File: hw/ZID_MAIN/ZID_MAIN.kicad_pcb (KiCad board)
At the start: 2 copper layers, 127 x 88.9 mm, 200 parts, among them J1 Conn 1x04 0.1" Socket, J10 FFC/FPC-40 Socket, J11 JST-PH-K B6B, J14 USB-C PWR ONLY, J2 JST-PH-K B6B, J3 Conn 1x02 0.1" pin, J4 Conn 1x03 0.1" pin, J5 Conn 1x08 0.1" pin, J6 Conn 1x08 0.1" pin, J7 Conn 2x04 0.1" pin, J8 Conn 2x02 0.1" pin, J9 Conn 2x04 0.1" pin, M1 WS-RP2040-Zero, SW1 SW_Push, SW2 SW_DIP_x02, U1 OSC-20MHz, U10 27WZ06, U11 74LVC125AS, U12 74LVC273, U13 74FCT2245, U14 AS7C1024B, U16 74FCT2245, U18 ATF1508AS, U2 74FCT2245, U20 74FCT2244, U22 ATF1504AS-44T, U23 74AHCT00, U24 74FCT2244, U25 ATF1504AS-44T, U26 ATF1504AS-44T, U27 ATF1504AS-44T, U28 ATF1504AS-44T, U3 24LC32, U4 MIC2775, U5 SST39SF010, U6 74LVC245, U7 74FCT2245, U8 74AHCT14, U9 Z80 C20MHz-PLCC

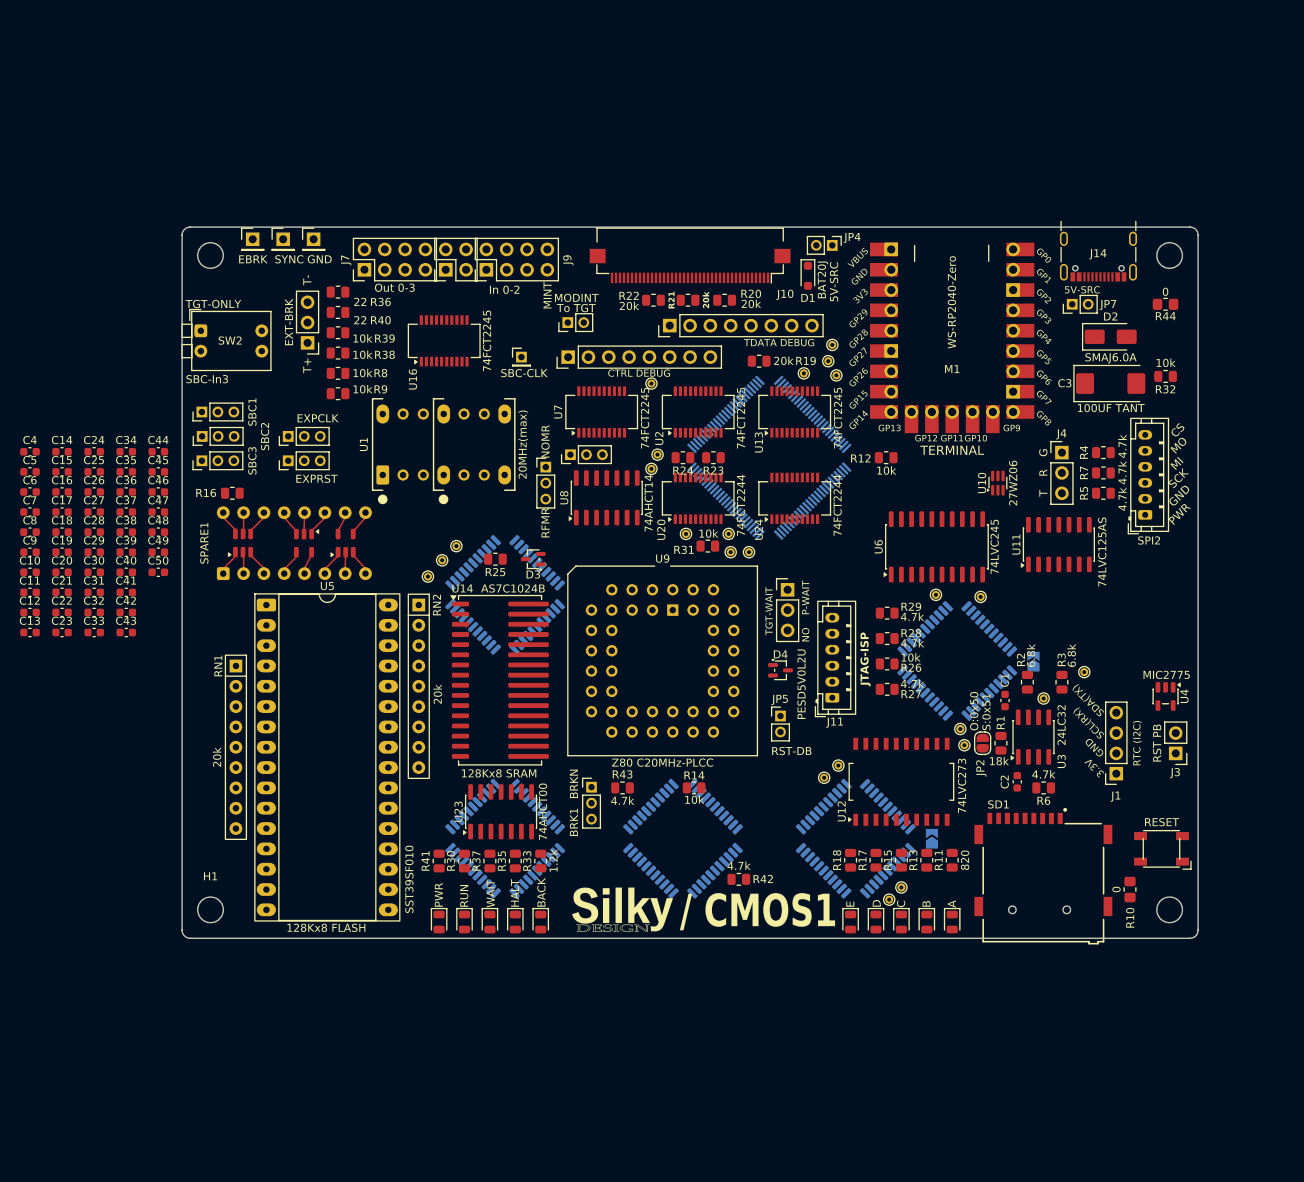
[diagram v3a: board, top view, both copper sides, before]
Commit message: SCHM: Updates per SM. PLD: comment corrections. PCB: start routing.
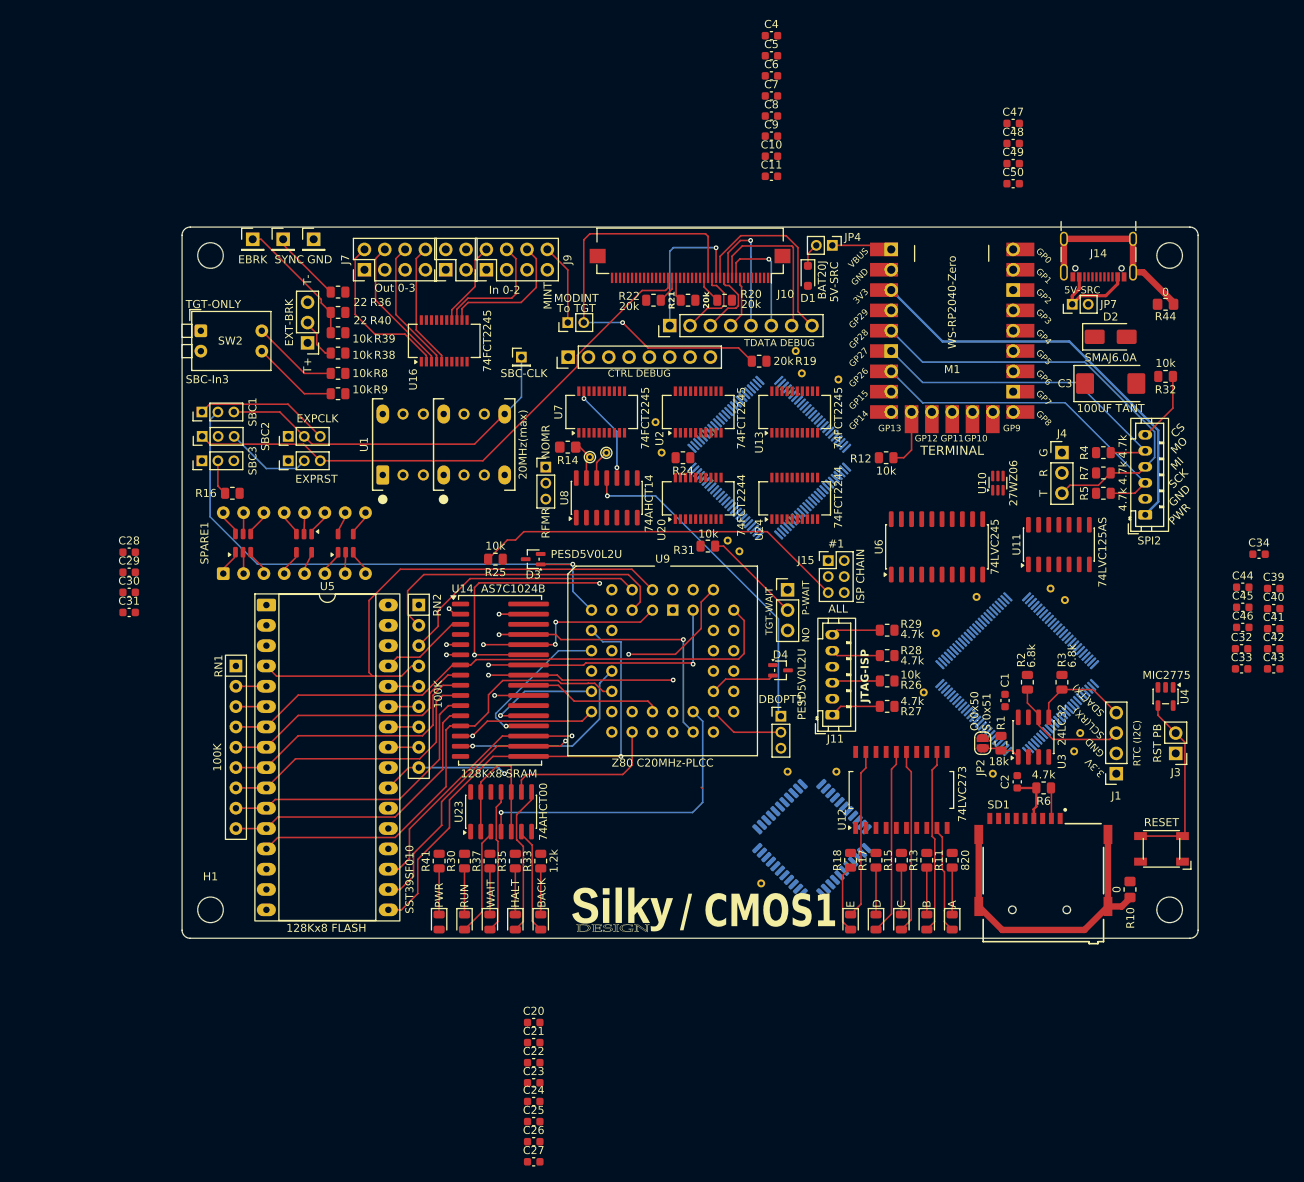
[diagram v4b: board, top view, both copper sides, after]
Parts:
- removed C12, C13, C14, C15, C16, C17, C18, C19, C35, C36, C37, C38: 0.1uF, Capacitor_SMD:C_0603_1608Metric
- removed JC1, JD1: SolderJumper_2_Open, Jumper:SolderJumper-2_P1.3mm_Open_TrianglePad1.0x1.5mm
- removed JP5: Jumper_2_Small_Bridged, Connector_PinHeader_2.00mm:PinHeader_1x02_P2.00mm_Vertical
- removed OP4: AES-Option_A-B_2mm, Connector_PinHeader_2.00mm:PinHeader_1x03_P2.00mm_Vertical
- removed R23: 10k, Resistor_SMD:R_0805_2012Metric
- removed R42, R43: 4.7k, Resistor_SMD:R_0805_2012Metric
- removed SPRU8F1: Conn_01x03_Pin, Connector_PinHeader_2.00mm:PinHeader_1x03_P2.00mm_Vertical
- removed TP12, TP26, TP28, TP29, TP31, TP32, TP33, TP34: TestPoint, TestPoint:TestPoint_THTPad_D1.0mm_Drill0.5mm
- removed U25, U26, U27, U28: ATF1504AS-44T, Package_QFP:TQFP-44_10x10mm_P0.8mm
- added DBOPT1: AES-Option_A-B_2mm, Connector_PinHeader_2.00mm:PinHeader_1x03_P2.00mm_Vertical, F.Cu at (133.6, 117.0)
- added J15: Conn 2x03 pin hdr 0.1", Connector_PinHeader_2.00mm:PinHeader_2x03_P2.00mm_Vertical, F.Cu at (139.5, 97.6)
- added TP19: TestPoint, TestPoint:TestPoint_THTPad_D1.0mm_Drill0.5mm, B.Cu at (170.2, 121.4)
- added TP20: TestPoint, TestPoint:TestPoint_THTPad_D1.0mm_Drill0.5mm, B.Cu at (134.4, 124.0)
- added TP23: TestPoint, TestPoint:TestPoint_THTPad_D1.0mm_Drill0.5mm, B.Cu at (160.1, 124.2)
- added TP24: TestPoint, TestPoint:TestPoint_THTPad_D1.0mm_Drill0.5mm, B.Cu at (153.0, 106.6)
- added U15: ATF1508AS, Package_QFP:TQFP-100_14x14mm_P0.5mm, B.Cu at (163.1, 111.8)
- R14: value 10k -> 100K; footprint Resistor_SMD:R_0805_2012Metric -> Resistor_SMD:R_0805_2012Metric_Pad1.20x1.40mm_HandSolder
- RN1, RN2: value 20k -> 100K
- TP10, TP11, TP13, TP17, TP18, TP2, TP21, TP22, TP25, TP4, TP5, TP6, TP8, TP9: moved to B.Cu
- moved C32 143.5 mm to (191.2, 108.6)
- moved C33 143.5 mm to (191.2, 111.1)
- moved C39 143.5 mm to (195.2, 101.1)
- moved C40 143.5 mm to (195.2, 103.6)
- moved C41 143.5 mm to (195.2, 106.1)
- moved C42 143.5 mm to (195.2, 108.6)
- moved C43 143.5 mm to (195.2, 111.1)
- moved C34 142.2 mm to (193.4, 96.8)
- moved C44 136.6 mm to (191.3, 100.9)
- moved C45 136.6 mm to (191.3, 103.4)
- moved C46 136.6 mm to (191.3, 105.9)
- moved C48 117.4 mm to (162.6, 45.4)
- moved C47 117.4 mm to (162.6, 42.9)
- moved C49 117.4 mm to (162.6, 47.9)
- moved C50 117.4 mm to (162.6, 50.5)
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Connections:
- net /MEM_OP- renamed /MEM_OP
- net Net-(JP7-A) renamed /VBUSP
- R14 pad 1: +5V -> Net-(R14-Pad1)
- R14 pad 2: Net-(JP5-B) -> +5V
- R25 pad 1: /PU -> +5V
- R25 pad 2: +5V -> /D2_IN
- R44 pad 1: Net-(J14-SHIELD-PadSH1) -> GND
- R44 pad 2: GND -> Net-(J14-SHIELD-PadSH1)
- TP10 pad 1: /IO85 -> Net-(U18-FMC89/IO)
- TP11 pad 1: /IO83 -> Net-(U18-FMC88/IO)
- TP13 pad 1: /IOBD24 -> Net-(U22-D41/IO/GCK3)
- TP17 pad 1: /ENBL_DOD -> Net-(U15-BMC22/IO)
- TP18 pad 1: /ADDR_DOD -> Net-(U15-HMC120/IO)
- TP21 pad 1: /IO8C -> Net-(U15-GMC107/IO)
- TP22 pad 1: /IO8D -> Net-(U22-CMC33/IO)
- TP25 pad 1: /IO10C -> Net-(U15-EMC80/IO)
- TP3 pad 1: /IO123 -> Net-(R14-Pad1)
- TP6 pad 1: /IO64 -> Net-(U15-H128/IO/GCK3)
- TP7 pad 1: /IO62 -> Net-(TP7-Pad1)
- U14 pad 30: /PU -> +5V
- U18 pad 12: /BRKN_AEQ- -> /BRKN_AEQ
- U18 pad 13: /BRK1_AEQ- -> /BRK1_AEQ
- U18 pad 27: /IO64 -> /ZID_IO
- U18 pad 28: /IO62 -> unconnected-(U18-DMC62/IO-Pad28)
- U18 pad 52: /IO81 -> unconnected-(U18-FMC81/IO-Pad52)
- U18 pad 53: /IO83 -> unconnected-(U18-FMC83/IO-Pad53)
- U18 pad 54: /IO85 -> unconnected-(U18-FMC85/IO-Pad54)
- U18 pad 55: /BA_CLK -> unconnected-(U18-FMC86/IO-Pad55)
- U18 pad 56: /AEN_CLR- -> Net-(U18-FMC88/IO)
- U18 pad 57: /AEN_CLK -> Net-(U18-FMC89/IO)
- U18 pad 58: /BA_CLR- -> unconnected-(U18-FMC91/IO-Pad58)
- U18 pad 60: /BRKPC_RD- -> unconnected-(U18-FMC93/IO-Pad60)
- U18 pad 61: /TGT_GO -> unconnected-(U18-FMC94/IO-Pad61)
- U18 pad 76: /BRKHWDET- -> unconnected-(U18-HMC115/IO-Pad76)
- U18 pad 77: /PCRD_DIN -> unconnected-(U18-HMC117/IO-Pad77)
- U18 pad 81: /IO123 -> unconnected-(U18-HMC123/IO-Pad81)
- U20 pad 11: Net-(U20-Ib1) -> +5V
- U20 pad 13: Net-(U20-Ib1) -> +5V
- U20 pad 15: Net-(U20-Ib1) -> +5V
- U22 pad 1: /JTD1O2I -> /JTD2O3I
- U22 pad 10: /IOBD25 -> /SBC_IO
- U22 pad 11: /IOBD24 -> /ZID_IO
- U22 pad 12: /ZA4 -> /ZA1
- U22 pad 13: /ZA3 -> /ZA0
- U22 pad 14: /ZA2 -> /ZA3
- U22 pad 15: /ZA1 -> /ZA2
- U22 pad 18: /SBC_IO -> Net-(U22-CMC33/IO)
- U22 pad 22: /ZD2 -> /ZD3
- U22 pad 23: /ZD4 -> /ZD5
- U22 pad 25: /ZD3 -> /ZD2
- U22 pad 27: /TGTMODE- -> /SBC_GPI2
- U22 pad 28: /IOBD51 -> /SBC_GPI3
- U22 pad 30: /SBC_GPI2 -> /SBC_GPI0
- U22 pad 31: /SBC_GPI3 -> /TGTMODE-
- U22 pad 32: /JTD2O3I -> /JTD3OCI
- U22 pad 33: /SBC_GPI1 -> Net-(U22-DMC57/IO)
- U22 pad 34: /TGT_GO -> /SBC_GPI1
- U22 pad 35: /SBC_GPI0 -> Net-(U22-D41/IO/GCK3)
- U22 pad 43: /SBC_GPO0 -> /SBC_GPO2
- U22 pad 44: /SBC_GPO2 -> /SBC_GPO0
- U22 pad 6: /ZD5 -> /ZD4
- U8 pad 12: Net-(SPRU8F1-Pin_3) -> Net-(TP7-Pad1)
- U8 pad 13: Net-(SPRU8F1-Pin_2) -> Net-(R14-Pad1)
- U9 pad 30: Net-(JP5-B) -> Net-(DBOPT1-C)
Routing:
- net /ZA1: track 0.00 -> 105.1 mm
- net /ZA0: track 0.00 -> 102.6 mm
- net /ZA3: track 0.00 -> 100.0 mm
- net /ZA2: track 0.00 -> 100.0 mm
- net /ZA4: track 0.00 -> 94.8 mm
- net /ZA10: track 0.00 -> 81.2 mm, vias 0 -> 2
- net /ZA5: track 0.00 -> 73.3 mm
- net /CLK: track 0.00 -> 72.0 mm, vias 0 -> 1
- net /TRST-: track 0.00 -> 70.5 mm
- net /ZA6: track 0.00 -> 70.0 mm, vias 0 -> 2
- net /ZA12: track 0.00 -> 67.9 mm
- net /ZD2: track 0.00 -> 65.6 mm, vias 0 -> 1
- net /ZA7: track 0.00 -> 65.4 mm, vias 0 -> 1
- net /ZD3: track 0.00 -> 60.2 mm, vias 0 -> 1
- net +3.3V: track 0.00 -> 58.2 mm
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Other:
- copper layers 2 -> 6
